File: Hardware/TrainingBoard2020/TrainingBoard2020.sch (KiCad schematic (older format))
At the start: 0 parts

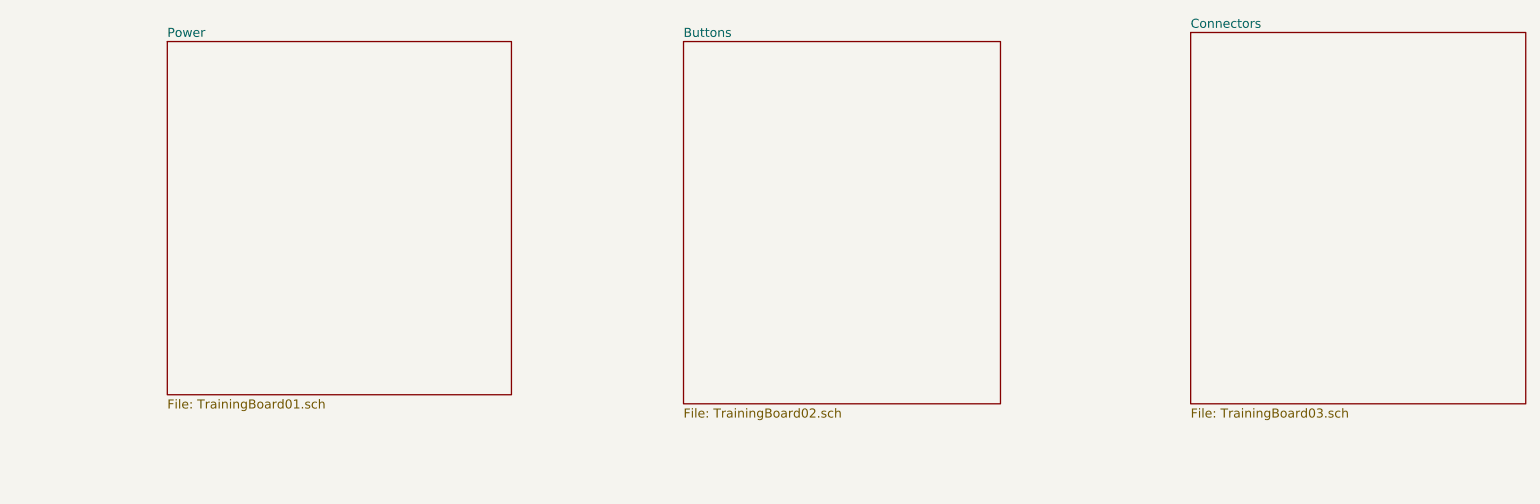
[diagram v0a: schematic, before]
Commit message: Started design layout of board
added copper GND layer and started layout and trace routing
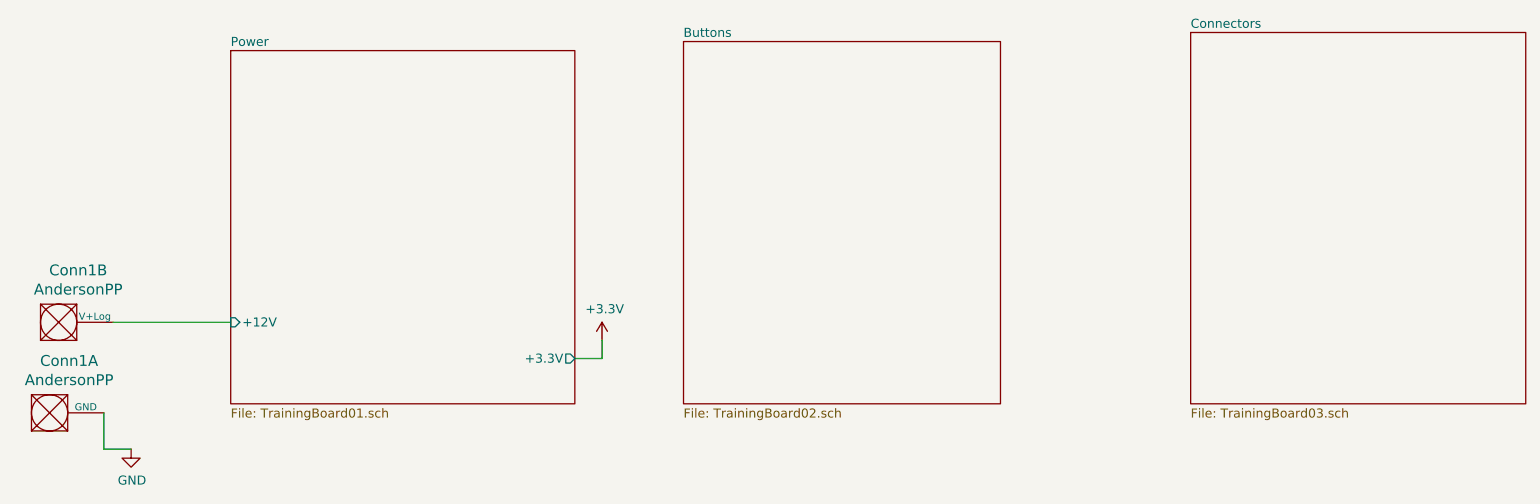
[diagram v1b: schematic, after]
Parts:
- added Conn1: AndersonPP, MRDT_Connectors:Anderson_2_Horizontal_Side_by_Side, symbol MRDT_Connectors:AndersonPP
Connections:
- new net GND: Conn1.1 (GND)
- new net Power/+12V: Conn1.2 (V+Log)
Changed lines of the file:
@@
 $EndDescr
 $Sheet
-S 1750 2450 1900 1950
+S 2100 2500 1900 1950
 U 5F567126
 F0 "Power" 50
 F1 "TrainingBoard01.sch" 50
+F2 "+12V" I L 2100 4000 50
+F3 "+3.3V" O R 4000 4200 50
 $EndSheet
 $Sheet
@@
 F1 "TrainingBoard03.sch" 50
 $EndSheet
+$Comp
+L MRDT_Connectors:AndersonPP Conn?
+U 1 1 5F66775C
+P 1000 4600
+AR Path="/5F56730D/5F66775C" Ref="Conn?"  Part="1"
+AR Path="/5F66775C" Ref="Conn1"  Part="1"
+F 0 "Conn1" H 1208 4987 60  0000 C CNN
+F 1 "AndersonPP" H 1208 4881 60  0000 C CNN
+F 2 "MRDT_Connectors:Anderson_2_Horizontal_Side_by_Side" H 850 4050 60  0001 C CNN
+F 3 "" H 850 4050 60  0001 C CNN
+	1    1000 4600
+	1    0    0    -1
+$EndComp
+$Comp
+L power:GND #PWR?
+U 1 1 5F667762
+P 1550 4700
+AR Path="/5F56730D/5F667762" Ref="#PWR?"  Part="1"
+AR Path="/5F667762" Ref="#PWR0101"  Part="1"
+F 0 "#PWR0101" H 1550 4450 50  0001 C CNN
+F 1 "GND" H 1555 4527 50  0000 C CNN
+F 2 "" H 1550 4700 50  0001 C CNN
+F 3 "" H 1550 4700 50  0001 C CNN
+	1    1550 4700
+	1    0    0    -1
+$EndComp
+$Comp
+L MRDT_Connectors:AndersonPP Conn?
+U 2 1 5F667768
+P 1050 4100
+AR Path="/5F56730D/5F667768" Ref="Conn?"  Part="2"
+AR Path="/5F667768" Ref="Conn1"  Part="2"
+F 0 "Conn1" H 1258 4487 60  0000 C CNN
+F 1 "AndersonPP" H 1258 4381 60  0000 C CNN
+F 2 "MRDT_Connectors:Anderson_2_Horizontal_Side_by_Side" H 900 3550 60  0001 C CNN
+F 3 "" H 900 3550 60  0001 C CNN
+	2    1050 4100
+	1    0    0    -1
+$EndComp
+Wire Wire Line
+	1400 4500 1400 4700
+Wire Wire Line
+	1400 4700 1550 4700
+Wire Wire Line
+	1450 4000 2100 4000
+$Comp
+L power:+3.3V #PWR0102
+U 1 1 5F66F575
+P 4150 4100
+F 0 "#PWR0102" H 4150 3950 50  0001 C CNN
+F 1 "+3.3V" H 4165 4273 50  0000 C CNN
+F 2 "" H 4150 4100 50  0001 C CNN
+F 3 "" H 4150 4100 50  0001 C CNN
+	1    4150 4100
+	1    0    0    -1
+$EndComp
+Wire Wire Line
+	4000 4200 4150 4200
+Wire Wire Line
+	4150 4200 4150 4100
 $EndSCHEMATC
